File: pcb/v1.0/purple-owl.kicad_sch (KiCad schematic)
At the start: 79 parts, among them SW1 SW_SPST, SW10 SW_SPST, SW11 SW_SPST, SW12 SW_SPST, SW13 SW_SPST, SW14 SW_SPST, SW15 SW_SPST, SW16 SW_SPST, SW17 SW_SPST, SW18 SW_SPST, SW19 SW_SPST, SW2 SW_SPST, SW20 SW_SPST, SW21 SW_SPST, SW22 SW_SPST, SW23 SW_SPST, SW24 SW_SPST, SW25 SW_SPST, SW26 SW_SPST, SW27 SW_SPST, SW28 SW_SPST, SW29 SW_SPST, SW3 SW_SPST, SW30 SW_SPST, SW31 SW_SPST, SW32 SW_SPST, SW33 SW_SPST, SW34 SW_SPST, SW35 SW_SPST, SW36 SW_SPST, SW37 SW_SPST, SW38 SW_SPST, SW39 SW_SPST, SW4 SW_SPST, SW40 SW_SPST, SW41 SW_SPST, SW42 SW_SPST, SW43 SW_SPST, SW44 SW_SPST, SW45 SW_SPST, SW46 SW_SPST, SW47 SW_SPST, SW48 SW_SPST, SW49 SW_SPST, SW5 SW_SPST, SW50 SW_SPST, SW51 SW_SPST, SW52 SW_SPST, SW53 SW_SPST, SW54 SW_SPST, SW55 SW_SPST, SW56 SW_SPST, SW57 SW_SPST, SW58 SW_SPST, SW59 SW_SPST, SW6 SW_SPST, SW60 SW_SPST, SW61 SW_SPST, SW7 SW_SPST, SW8 SW_SPST, SW9 SW_SPST, U1 74HC165, U2 74HC165, U3 74HC165, U4 74HC165, U5 74HC165, U6 74HC165, U7 74HC165, U8 74HC165, U9 Adafruit_QTPy_RP2040

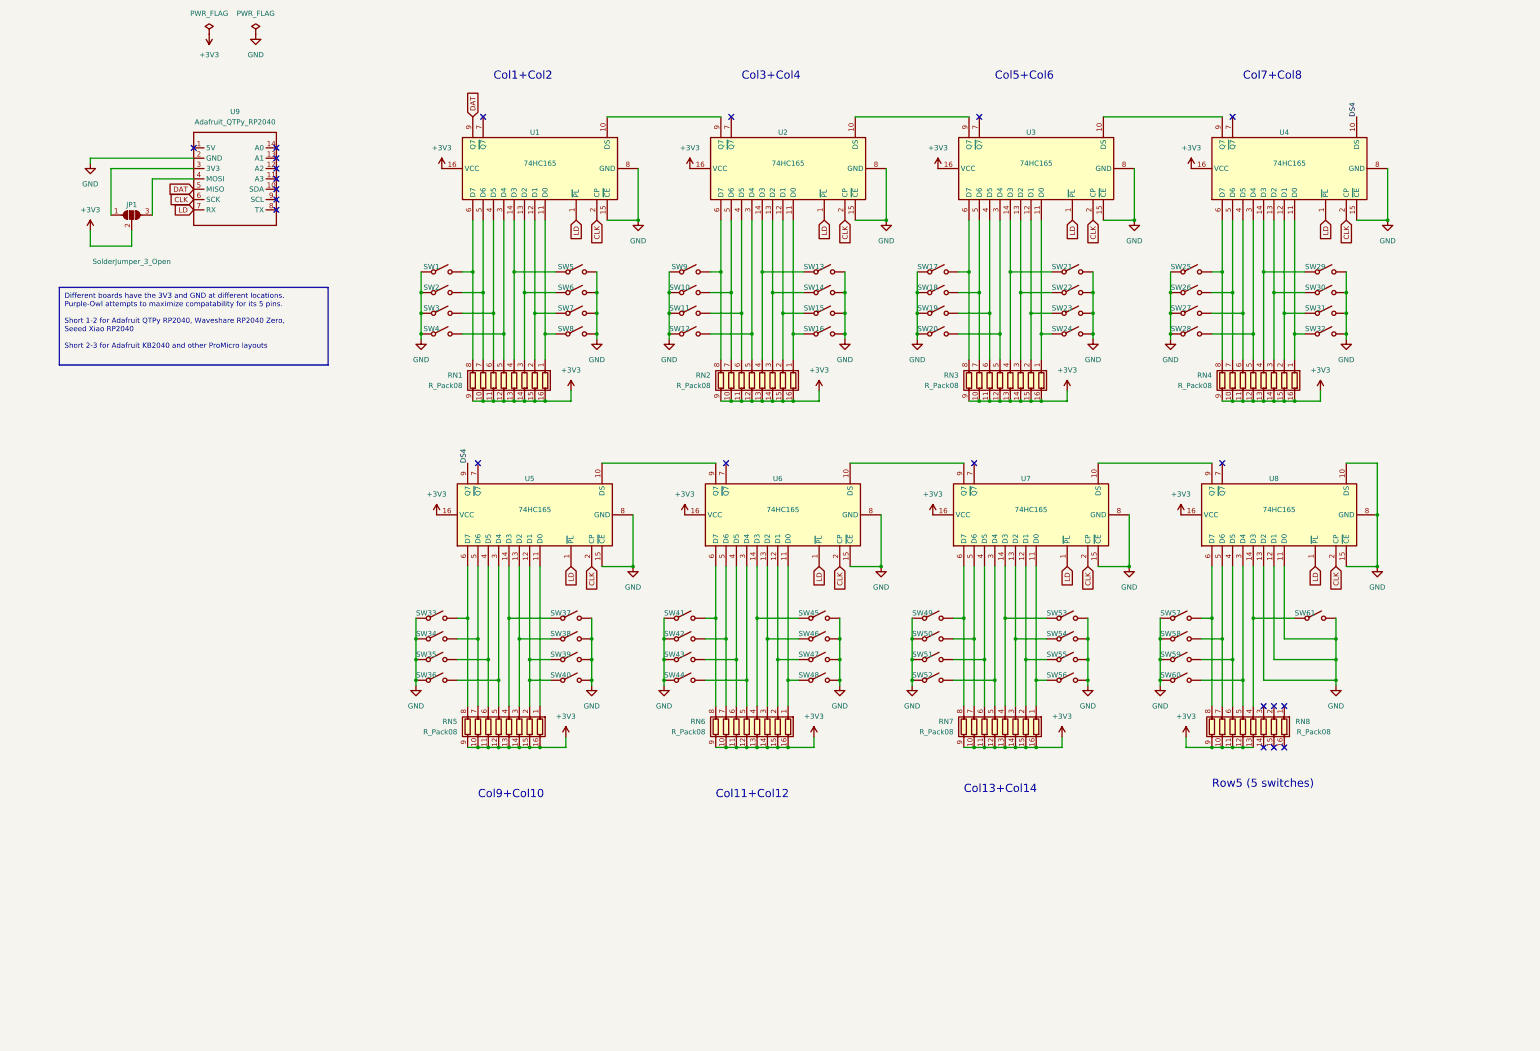
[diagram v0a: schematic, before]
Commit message: Update 1.0 Schematic
- Add 16 underglow LEDs (ws2812b-v5)
- Jumper for LED power source (3.3V or 5V)
- Add footprints for jumpers
  - ComboJumper: through-hole/solder combo jumper
  - SolderJumper: regular solder jumper with mask between pads
- Update README
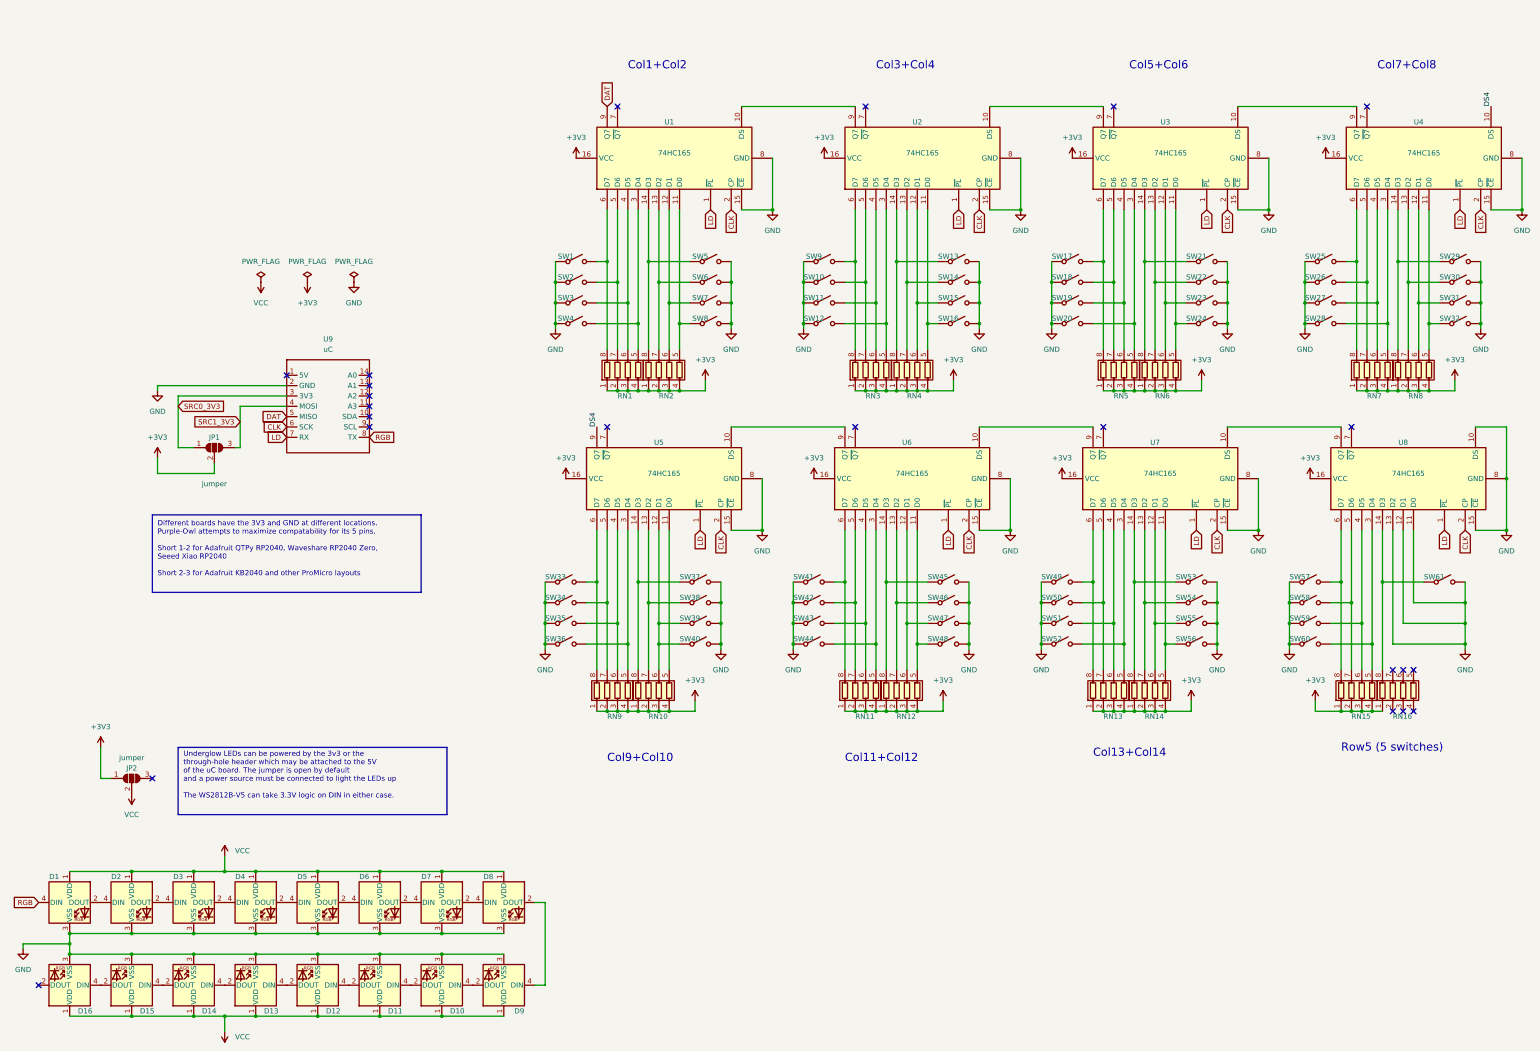
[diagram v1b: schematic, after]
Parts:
- removed RN1, RN2, RN3, RN4, RN5, RN6, RN7, RN8: R_Pack08, symbol Device:R_Pack08
- added D1, D10, D11, D12, D13, D14, D15, D16, D2, D3, D4, D5, D6, D7, D8, D9: WS2812B, purple-owl:WS2812B, symbol LED:WS2812B
- added JP2: jumper, purple-owl:ComboJumper, symbol Jumper:SolderJumper_3_Open
- added RN1, RN10, RN11, RN12, RN13, RN14, RN15, RN16, RN2, RN3, RN4, RN5, RN6, RN7, RN8, RN9: R_Pack04, Resistor_SMD:R_Array_Convex_4x0402, symbol Device:R_Pack04
- JP1: value SolderJumper_3_Open -> jumper; footprint (none) -> purple-owl:ComboJumper
- SW1, SW10, SW11, SW12, SW13, SW14, SW15, SW16, SW17, SW18, SW19, SW2, SW20, SW21, SW22, SW23, SW24, SW25, SW26, SW27, SW28, SW29, SW3, SW30, SW31, SW32, SW33, SW34, SW35, SW36, SW37, SW38, SW39, SW4, SW40, SW41, SW42, SW43, SW44, SW45, SW46, SW47, SW48, SW49, SW5, SW50, SW51, SW52, SW53, SW54, SW55, SW56, SW57, SW58, SW6, SW60, SW61, SW7, SW8, SW9: footprint (none) -> acheron:MX100H
- SW59: footprint (none) -> acheron:MX200HR
- U1, U2, U3, U4, U5, U6, U7, U8: footprint (none) -> Package_SO:TSSOP-16_4.4x5mm_P0.65mm
- U9: value Adafruit_QTPy_RP2040 -> uC; footprint (none) -> purple-owl:Adafruit_QTPy_RP2040_alt
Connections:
- net +3V3: now also JP2.1 (A), RN1.1 (R1.1), RN1.2 (R2.1), RN1.3 (R3.1), RN1.4 (R4.1), RN10.1 (R1.1), RN10.2 (R2.1), RN10.3 (R3.1), RN10.4 (R4.1), RN11.1 (R1.1), RN11.2 (R2.1), RN11.3 (R3.1), RN11.4 (R4.1), RN12.1 (R1.1), RN12.2 (R2.1), RN12.3 (R3.1), RN12.4 (R4.1), RN13.1 (R1.1), RN13.2 (R2.1), RN13.3 (R3.1), RN13.4 (R4.1), RN14.1 (R1.1), RN14.2 (R2.1), RN14.3 (R3.1), RN14.4 (R4.1), RN15.1 (R1.1), RN15.2 (R2.1), RN15.3 (R3.1), RN15.4 (R4.1), RN16.1 (R1.1), RN2.1 (R1.1), RN2.2 (R2.1), RN2.3 (R3.1), RN2.4 (R4.1), RN3.1 (R1.1), RN3.2 (R2.1), RN3.3 (R3.1), RN3.4 (R4.1), RN4.1 (R1.1), RN4.2 (R2.1), RN4.3 (R3.1), RN4.4 (R4.1), RN5.1 (R1.1), RN5.2 (R2.1), RN5.3 (R3.1), RN5.4 (R4.1), RN6.1 (R1.1), RN6.2 (R2.1), RN6.3 (R3.1), RN6.4 (R4.1), RN7.1 (R1.1), RN7.2 (R2.1), RN7.3 (R3.1), RN7.4 (R4.1), RN8.1 (R1.1), RN8.2 (R2.1), RN8.3 (R3.1), RN8.4 (R4.1), RN9.1 (R1.1), RN9.2 (R2.1), RN9.3 (R3.1), RN9.4 (R4.1)
- net GND: now also D1.3 (VSS), D10.3 (VSS), D11.3 (VSS), D12.3 (VSS), D13.3 (VSS), D14.3 (VSS), D15.3 (VSS), D16.3 (VSS), D2.3 (VSS), D3.3 (VSS), D4.3 (VSS), D5.3 (VSS), D6.3 (VSS), D7.3 (VSS), D8.3 (VSS), D9.3 (VSS)
- net at SW50.2 (B), U7.5 (D6): now also RN13.7 (R2.2)
- net at SW35.2 (B), U5.4 (D5): now also RN9.6 (R3.2)
- net SRC0_3V3: now reaches JP1.1 (A), U9.3 (3V3)
- net SRC1_3V3: now reaches JP1.3 (B), U9.4 (MOSI)
- net at SW32.1 (A), U4.11 (D0): now also RN8.5 (R4.2)
- net at SW31.1 (A), U4.12 (D1): now also RN8.6 (R3.2)
- net at SW30.1 (A), U4.13 (D2): now also RN8.7 (R2.2)
- net at SW29.1 (A), U4.14 (D3): now also RN8.8 (R1.2)
- net at SW28.2 (B), U4.3 (D4): now also RN7.5 (R4.2)
- net at SW27.2 (B), U4.4 (D5): now also RN7.6 (R3.2)
- net at SW26.2 (B), U4.5 (D6): now also RN7.7 (R2.2)
- net at SW25.2 (B), U4.6 (D7): now also RN7.8 (R1.2)
- net at SW21.1 (A), U3.14 (D3): now also RN6.8 (R1.2)
- net at SW6.1 (A), U1.13 (D2): now also RN2.7 (R2.2)
- net at SW45.1 (A), U6.14 (D3): now also RN12.8 (R1.2)
- net at SW46.1 (A), U6.13 (D2): now also RN12.7 (R2.2)
- net at SW13.1 (A), U2.14 (D3): now also RN4.8 (R1.2)
- net at SW59.2 (B), U8.4 (D5): now also RN15.6 (R3.2)
- net at SW24.1 (A), U3.11 (D0): now also RN6.5 (R4.2)
- net at SW23.1 (A), U3.12 (D1): now also RN6.6 (R3.2)
- net at SW22.1 (A), U3.13 (D2): now also RN6.7 (R2.2)
- net at SW20.2 (B), U3.3 (D4): now also RN5.5 (R4.2)
- net at SW19.2 (B), U3.4 (D5): now also RN5.6 (R3.2)
- net at SW18.2 (B), U3.5 (D6): now also RN5.7 (R2.2)
- net at SW17.2 (B), U3.6 (D7): now also RN5.8 (R1.2)
- net at SW14.1 (A), U2.13 (D2): now also RN4.7 (R2.2)
- net at SW37.1 (A), U5.14 (D3): now also RN10.8 (R1.2)
- net at SW16.1 (A), U2.11 (D0): now also RN4.5 (R4.2)
- net at SW15.1 (A), U2.12 (D1): now also RN4.6 (R3.2)
- net at SW12.2 (B), U2.3 (D4): now also RN3.5 (R4.2)
- net at SW11.2 (B), U2.4 (D5): now also RN3.6 (R3.2)
- net at SW10.2 (B), U2.5 (D6): now also RN3.7 (R2.2)
- net at SW9.2 (B), U2.6 (D7): now also RN3.8 (R1.2)
- net at SW4.2 (B), U1.3 (D4): now also RN1.5 (R4.2)
- net at SW60.2 (B), U8.3 (D4): now also RN15.5 (R4.2)
- net at SW56.1 (A), U7.11 (D0): now also RN14.5 (R4.2)
- net at SW8.1 (A), U1.11 (D0): now also RN2.5 (R4.2)
- net at SW7.1 (A), U1.12 (D1): now also RN2.6 (R3.2)
- net at SW5.1 (A), U1.14 (D3): now also RN2.8 (R1.2)
- net at SW3.2 (B), U1.4 (D5): now also RN1.6 (R3.2)
- net at SW2.2 (B), U1.5 (D6): now also RN1.7 (R2.2)
- net at SW1.2 (B), U1.6 (D7): now also RN1.8 (R1.2)
- net RGB: now reaches U9.8 (TX)
- net RGB: now also D1.4 (DIN)
- net at SW61.1 (A), U8.14 (D3): now also RN16.8 (R1.2)
- net at SW58.2 (B), U8.5 (D6): now also RN15.7 (R2.2)
- net at SW57.2 (B), U8.6 (D7): now also RN15.8 (R1.2)
- net at SW49.2 (B), U7.6 (D7): now also RN13.8 (R1.2)
- net at SW39.1 (A), SW40.1 (A), U5.12 (D1): now also RN10.6 (R3.2)
- net at SW44.2 (B), U6.3 (D4): now also RN11.5 (R4.2)
- net at SW41.2 (B), U6.6 (D7): now also RN11.8 (R1.2)
- net at SW48.1 (A), U6.11 (D0): now also RN12.5 (R4.2)
- net at SW38.1 (A), U5.13 (D2): now also RN10.7 (R2.2)
- net at SW52.2 (B), U7.3 (D4): now also RN13.5 (R4.2)
- net at SW55.1 (A), U7.12 (D1): now also RN14.6 (R3.2)
- net at SW54.1 (A), U7.13 (D2): now also RN14.7 (R2.2)
- net at SW53.1 (A), U7.14 (D3): now also RN14.8 (R1.2)
- net at SW51.2 (B), U7.4 (D5): now also RN13.6 (R3.2)
- net at SW47.1 (A), U6.12 (D1): now also RN12.6 (R3.2)
- net at SW43.2 (B), U6.4 (D5): now also RN11.6 (R3.2)
- net at SW42.2 (B), U6.5 (D6): now also RN11.7 (R2.2)
- net at SW36.2 (B), U5.3 (D4): now also RN9.5 (R4.2)
- net at U5.11 (D0): now also RN10.5 (R4.2)
- net at SW34.2 (B), U5.5 (D6): now also RN9.7 (R2.2)
- net at SW33.2 (B), U5.6 (D7): now also RN9.8 (R1.2)
- new net: D10.2 (DOUT), D11.4 (DIN)
- new net: D10.4 (DIN), D9.2 (DOUT)
- new net: D11.2 (DOUT), D12.4 (DIN)
- new net: D8.2 (DOUT), D9.4 (DIN)
- new net: D2.2 (DOUT), D3.4 (DIN)
- new net: D1.2 (DOUT), D2.4 (DIN)
- new net: D15.2 (DOUT), D16.4 (DIN)
- new net: D3.2 (DOUT), D4.4 (DIN)
- new net: D12.2 (DOUT), D13.4 (DIN)
- new net: D4.2 (DOUT), D5.4 (DIN)
- new net: D14.2 (DOUT), D15.4 (DIN)
- new net: D13.2 (DOUT), D14.4 (DIN)
- new net: D5.2 (DOUT), D6.4 (DIN)
- new net: D6.2 (DOUT), D7.4 (DIN)
- new net: D7.2 (DOUT), D8.4 (DIN)
- new net VCC: D1.1 (VDD), D10.1 (VDD), D11.1 (VDD), D12.1 (VDD), D13.1 (VDD), D14.1 (VDD), D15.1 (VDD), D16.1 (VDD), D2.1 (VDD), D3.1 (VDD), D4.1 (VDD), D5.1 (VDD), D6.1 (VDD), D7.1 (VDD), D8.1 (VDD), D9.1 (VDD), JP2.2 (C)
- no-connect marks 22 -> 23
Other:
- note added: "Underglow LEDs can be powered by the 3v3 or the through-hole header which may be attached to the 5V of the uC board. The jumper is open by default and a power source must be connected to light the LEDs up The WS2812B-V5 can take 3.3V logic on DIN in either case."
- moved on the sheet: JP1, SW1, SW10, SW11, SW12, SW13, SW14, SW15, SW16, SW17, SW18, SW19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

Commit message: Push towards v1.0
- Layout for v1.0
- Fab files for Seeed and JLCPCB
- Updated footprints
- Updated README
- Update JLCPCB position fix script
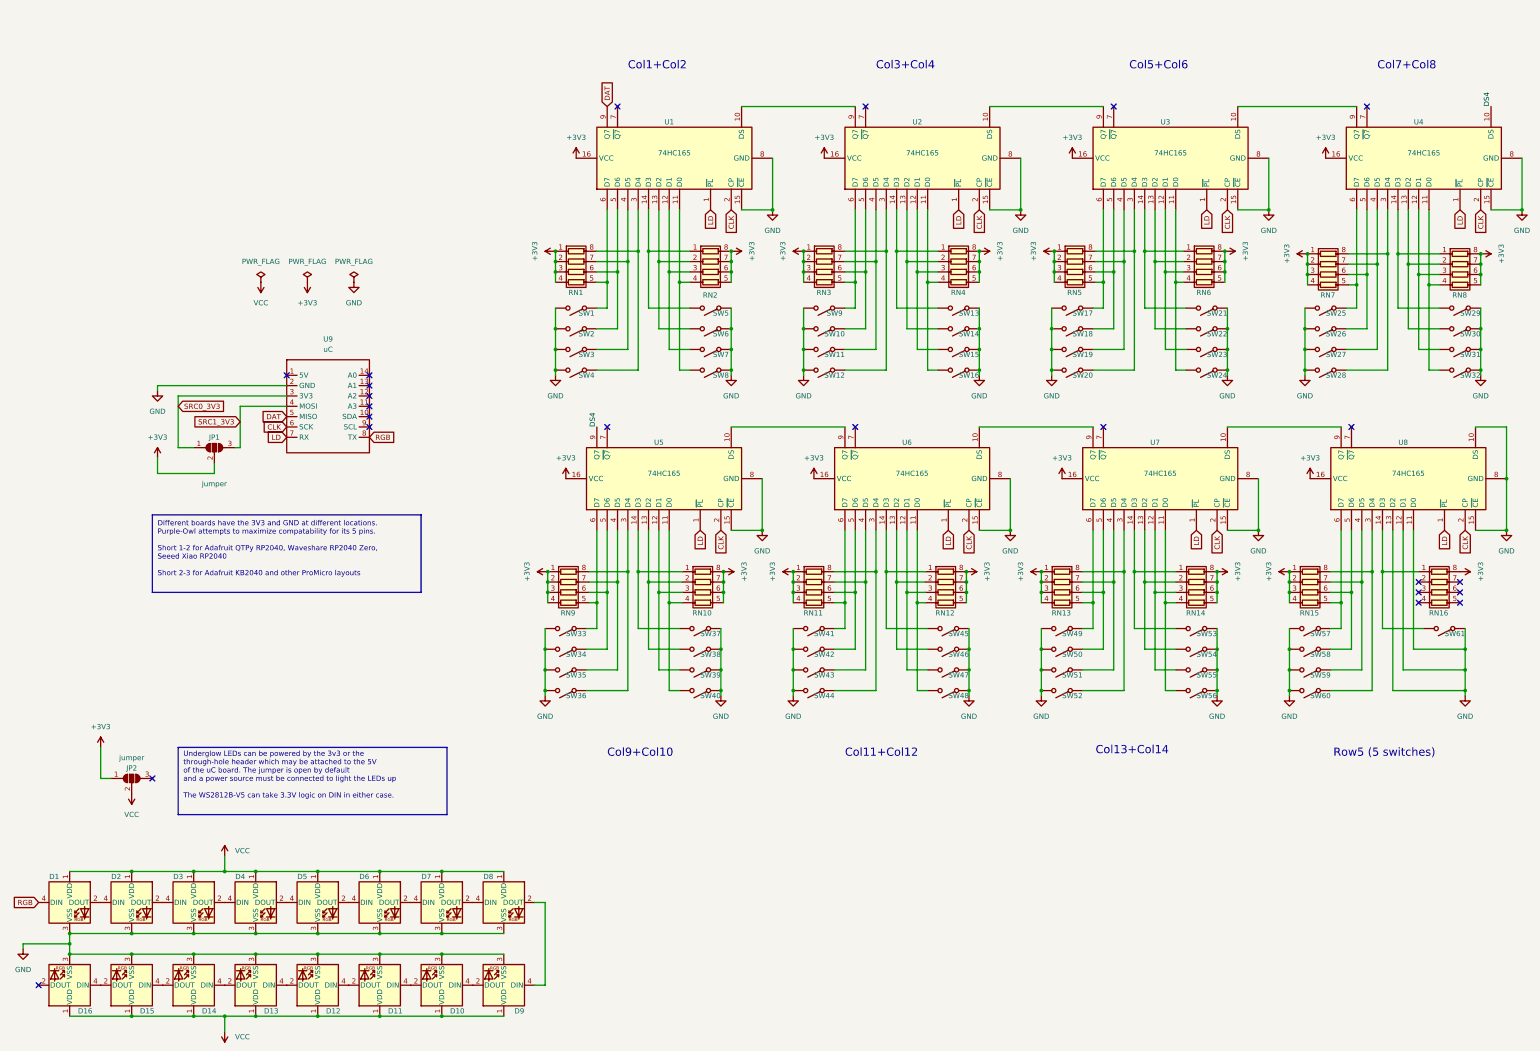
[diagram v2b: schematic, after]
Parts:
- JP1, JP2: footprint purple-owl:ComboJumper -> purple-owl:Jumper3
- RN1, RN10, RN11, RN12, RN13, RN14, RN15, RN16, RN2, RN3, RN4, RN5, RN6, RN7, RN8, RN9: footprint Resistor_SMD:R_Array_Convex_4x0402 -> Resistor_SMD:R_Array_Convex_4x0603
- U9: footprint purple-owl:Adafruit_QTPy_RP2040_alt -> purple-owl:purple_owl_uC
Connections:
- net +3V3: now also RN10.5 (R4.2), RN10.6 (R3.2), RN10.7 (R2.2), RN10.8 (R1.2), RN12.5 (R4.2), RN12.6 (R3.2), RN12.7 (R2.2), RN12.8 (R1.2), RN14.5 (R4.2), RN14.6 (R3.2), RN14.7 (R2.2), RN14.8 (R1.2), RN16.8 (R1.2), RN2.5 (R4.2), RN2.6 (R3.2), RN2.7 (R2.2), RN2.8 (R1.2), RN4.5 (R4.2), RN4.6 (R3.2), RN4.7 (R2.2), RN4.8 (R1.2), RN6.5 (R4.2), RN6.6 (R3.2), RN6.7 (R2.2), RN6.8 (R1.2), RN8.5 (R4.2), RN8.6 (R3.2), RN8.7 (R2.2), RN8.8 (R1.2); no longer RN10.1 (R1.1), RN10.2 (R2.1), RN10.3 (R3.1), RN10.4 (R4.1), RN12.1 (R1.1), RN12.2 (R2.1), RN12.3 (R3.1), RN12.4 (R4.1), RN14.1 (R1.1), RN14.2 (R2.1), RN14.3 (R3.1), RN14.4 (R4.1), RN16.1 (R1.1), RN2.1 (R1.1), RN2.2 (R2.1), RN2.3 (R3.1), RN2.4 (R4.1), RN4.1 (R1.1), RN4.2 (R2.1), RN4.3 (R3.1), RN4.4 (R4.1), RN6.1 (R1.1), RN6.2 (R2.1), RN6.3 (R3.1), RN6.4 (R4.1), RN8.1 (R1.1), RN8.2 (R2.1), RN8.3 (R3.1), RN8.4 (R4.1)
- net GND: now also SW1.2 (B), SW10.2 (B), SW11.2 (B), SW12.2 (B), SW13.1 (A), SW14.1 (A), SW15.1 (A), SW16.1 (A), SW17.2 (B), SW18.2 (B), SW19.2 (B), SW2.2 (B), SW20.2 (B), SW21.1 (A), SW22.1 (A), SW23.1 (A), SW24.1 (A), SW25.2 (B), SW26.2 (B), SW27.2 (B), SW28.2 (B), SW29.1 (A), SW3.2 (B), SW30.1 (A), SW31.1 (A), SW32.1 (A), SW33.2 (B), SW34.2 (B), SW35.2 (B), SW36.2 (B), SW37.1 (A), SW38.1 (A), SW39.1 (A), SW4.2 (B), SW40.1 (A), SW41.2 (B), SW42.2 (B), SW43.2 (B), SW44.2 (B), SW45.1 (A), SW46.1 (A), SW47.1 (A), SW48.1 (A), SW49.2 (B), SW5.1 (A), SW50.2 (B), SW51.2 (B), SW52.2 (B), SW53.1 (A), SW54.1 (A), SW55.1 (A), SW56.1 (A), SW57.2 (B), SW58.2 (B), SW59.2 (B), SW6.1 (A), SW60.2 (B), SW61.1 (A), SW7.1 (A), SW8.1 (A), SW9.2 (B); no longer SW1.1 (A), SW10.1 (A), SW11.1 (A), SW12.1 (A), SW13.2 (B), SW14.2 (B), SW15.2 (B), SW16.2 (B), SW17.1 (A), SW18.1 (A), SW19.1 (A), SW2.1 (A), SW20.1 (A), SW21.2 (B), SW22.2 (B), SW23.2 (B), SW24.2 (B), SW25.1 (A), SW26.1 (A), SW27.1 (A), SW28.1 (A), SW29.2 (B), SW3.1 (A), SW30.2 (B), SW31.2 (B), SW32.2 (B), SW33.1 (A), SW34.1 (A), SW35.1 (A), SW36.1 (A), SW37.2 (B), SW38.2 (B), SW39.2 (B), SW4.1 (A), SW40.2 (B), SW41.1 (A), SW42.1 (A), SW43.1 (A), SW44.1 (A), SW45.2 (B), SW46.2 (B), SW47.2 (B), SW48.2 (B), SW49.1 (A), SW5.2 (B), SW50.1 (A), SW51.1 (A), SW52.1 (A), SW53.2 (B), SW54.2 (B), SW55.2 (B), SW56.2 (B), SW57.1 (A), SW58.1 (A), SW59.1 (A), SW6.2 (B), SW60.1 (A), SW61.2 (B), SW7.2 (B), SW8.2 (B), SW9.1 (A)
- net at U5.11 (D0): now also RN10.4 (R4.1), SW40.2 (B); no longer RN10.5 (R4.2)
- new net: RN13.6 (R3.2), SW50.1 (A), U7.5 (D6)
- new net: RN9.7 (R2.2), SW35.1 (A), U5.4 (D5)
- new net: RN5.5 (R4.2), SW17.1 (A), U3.6 (D7)
- new net: RN5.6 (R3.2), SW18.1 (A), U3.5 (D6)
- new net: RN5.7 (R2.2), SW19.1 (A), U3.4 (D5)
- new net: RN5.8 (R1.2), SW20.1 (A), U3.3 (D4)
- new net: RN8.4 (R4.1), SW32.2 (B), U4.11 (D0)
- new net: RN8.3 (R3.1), SW31.2 (B), U4.12 (D1)
- new net: RN8.2 (R2.1), SW30.2 (B), U4.13 (D2)
- new net: RN8.1 (R1.1), SW29.2 (B), U4.14 (D3)
- new net: RN7.8 (R1.2), SW28.1 (A), U4.3 (D4)
- new net: RN7.7 (R2.2), SW27.1 (A), U4.4 (D5)
- new net: RN7.6 (R3.2), SW26.1 (A), U4.5 (D6)
- new net: RN7.5 (R4.2), SW25.1 (A), U4.6 (D7)
- new net: RN6.1 (R1.1), SW21.2 (B), U3.14 (D3)
- new net: RN15.5 (R4.2), SW57.1 (A), U8.6 (D7)
- new net: RN15.6 (R3.2), SW58.1 (A), U8.5 (D6)
- new net: RN15.7 (R2.2), SW59.1 (A), U8.4 (D5)
- new net: RN15.8 (R1.2), SW60.1 (A), U8.3 (D4)
- new net: RN2.2 (R2.1), SW6.2 (B), U1.13 (D2)
- new net: RN6.2 (R2.1), SW22.2 (B), U3.13 (D2)
- new net: RN6.3 (R3.1), SW23.2 (B), U3.12 (D1)
- new net: RN6.4 (R4.1), SW24.2 (B), U3.11 (D0)
- new net: RN12.1 (R1.1), SW45.2 (B), U6.14 (D3)
- new net: RN12.2 (R2.1), SW46.2 (B), U6.13 (D2)
- new net: RN4.1 (R1.1), SW13.2 (B), U2.14 (D3)
- new net: RN4.2 (R2.1), SW14.2 (B), U2.13 (D2)
- new net: RN10.1 (R1.1), SW37.2 (B), U5.14 (D3)
- new net: RN1.8 (R1.2), SW4.1 (A), U1.3 (D4)
- new net: RN3.6 (R3.2), SW10.1 (A), U2.5 (D6)
- new net: RN14.4 (R4.1), SW56.2 (B), U7.11 (D0)
- new net: RN13.5 (R4.2), SW49.1 (A), U7.6 (D7)
- new net: RN11.5 (R4.2), SW41.1 (A), U6.6 (D7)
- new net: RN11.6 (R3.2), SW42.1 (A), U6.5 (D6)
- new net: RN11.7 (R2.2), SW43.1 (A), U6.4 (D5)
- new net: RN11.8 (R1.2), SW44.1 (A), U6.3 (D4)
- new net: RN4.4 (R4.1), SW16.2 (B), U2.11 (D0)
- new net: RN4.3 (R3.1), SW15.2 (B), U2.12 (D1)
- new net: RN3.8 (R1.2), SW12.1 (A), U2.3 (D4)
- new net: RN3.7 (R2.2), SW11.1 (A), U2.4 (D5)
- new net: RN3.5 (R4.2), SW9.1 (A), U2.6 (D7)
- new net: RN10.3 (R3.1), SW39.2 (B), U5.12 (D1)
- new net: RN12.3 (R3.1), SW47.2 (B), U6.12 (D1)
- new net: RN12.4 (R4.1), SW48.2 (B), U6.11 (D0)
- new net: RN14.1 (R1.1), SW53.2 (B), U7.14 (D3)
- new net: RN14.2 (R2.1), SW54.2 (B), U7.13 (D2)
- new net: RN14.3 (R3.1), SW55.2 (B), U7.12 (D1)
- new net: RN2.4 (R4.1), SW8.2 (B), U1.11 (D0)
- new net: RN2.3 (R3.1), SW7.2 (B), U1.12 (D1)
- new net: RN2.1 (R1.1), SW5.2 (B), U1.14 (D3)
- new net: RN1.7 (R2.2), SW3.1 (A), U1.4 (D5)
- new net: RN1.6 (R3.2), SW2.1 (A), U1.5 (D6)
- new net: RN1.5 (R4.2), SW1.1 (A), U1.6 (D7)
- new net: RN10.2 (R2.1), SW38.2 (B), U5.13 (D2)
- new net: RN13.8 (R1.2), SW52.1 (A), U7.3 (D4)
- new net: RN13.7 (R2.2), SW51.1 (A), U7.4 (D5)
- new net: RN9.8 (R1.2), SW36.1 (A), U5.3 (D4)
- new net: RN9.5 (R4.2), SW33.1 (A), U5.6 (D7)
- new net: RN9.6 (R3.2), SW34.1 (A), U5.5 (D6)
- new net: RN16.1 (R1.1), SW61.2 (B), U8.14 (D3)
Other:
- moved on the sheet: RN10, RN11, RN12, RN13, RN14, RN15, RN16, RN3, RN4, RN5, RN6, RN7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
